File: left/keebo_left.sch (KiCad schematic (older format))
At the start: 56 parts, among them SW1 SW_Push, SW10 SW_Push, SW11 SW_Push, SW12 SW_Push, SW13 SW_Push, SW14 SW_Push, SW17 SW_Push, SW18 SW_Push, SW19 SW_Push, SW2 SW_Push, SW20 SW_Push, SW21 SW_Push, SW22 SW_Push, SW25 SW_Push, SW26 SW_Push, SW27 SW_Push, SW28 SW_Push, SW29 SW_Push, SW3 SW_Push, SW30 SW_Push, SW34 SW_Push, SW35 SW_Push, SW36 SW_Push, SW4 SW_Push, SW5 SW_Push, SW6 SW_Push, SW7 SW_Push, SW9 SW_Push

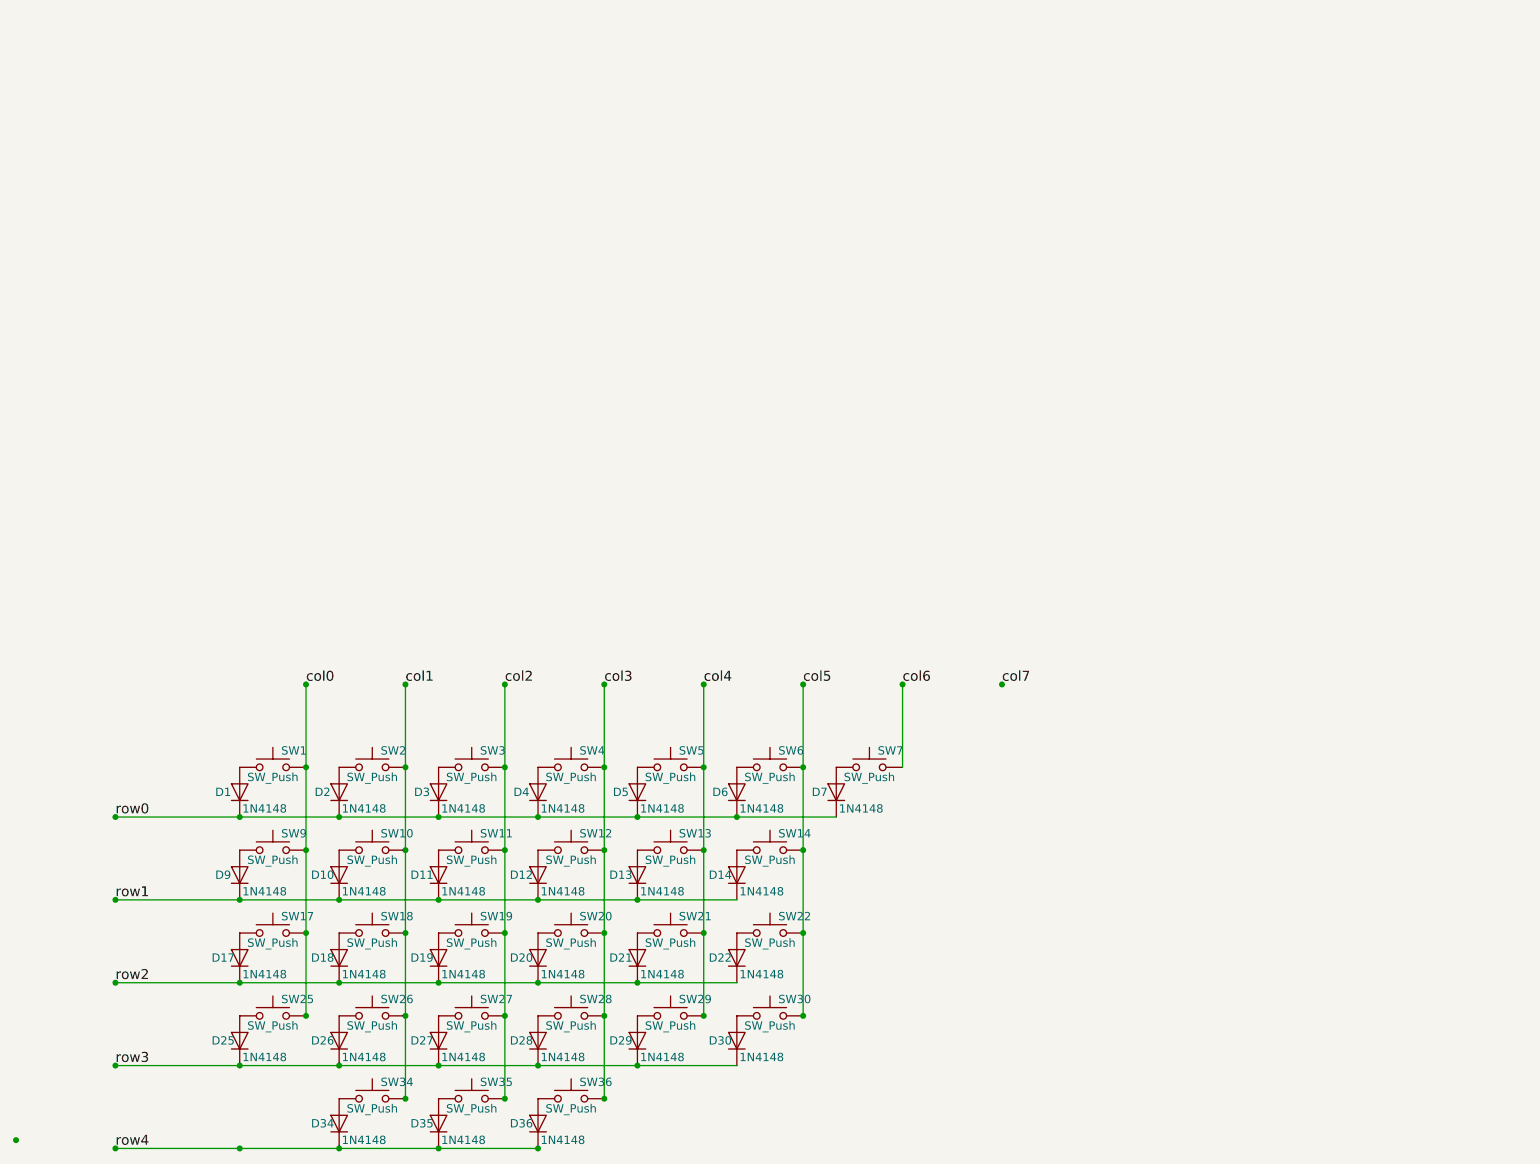
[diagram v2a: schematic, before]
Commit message: Create PCB for low profile switches
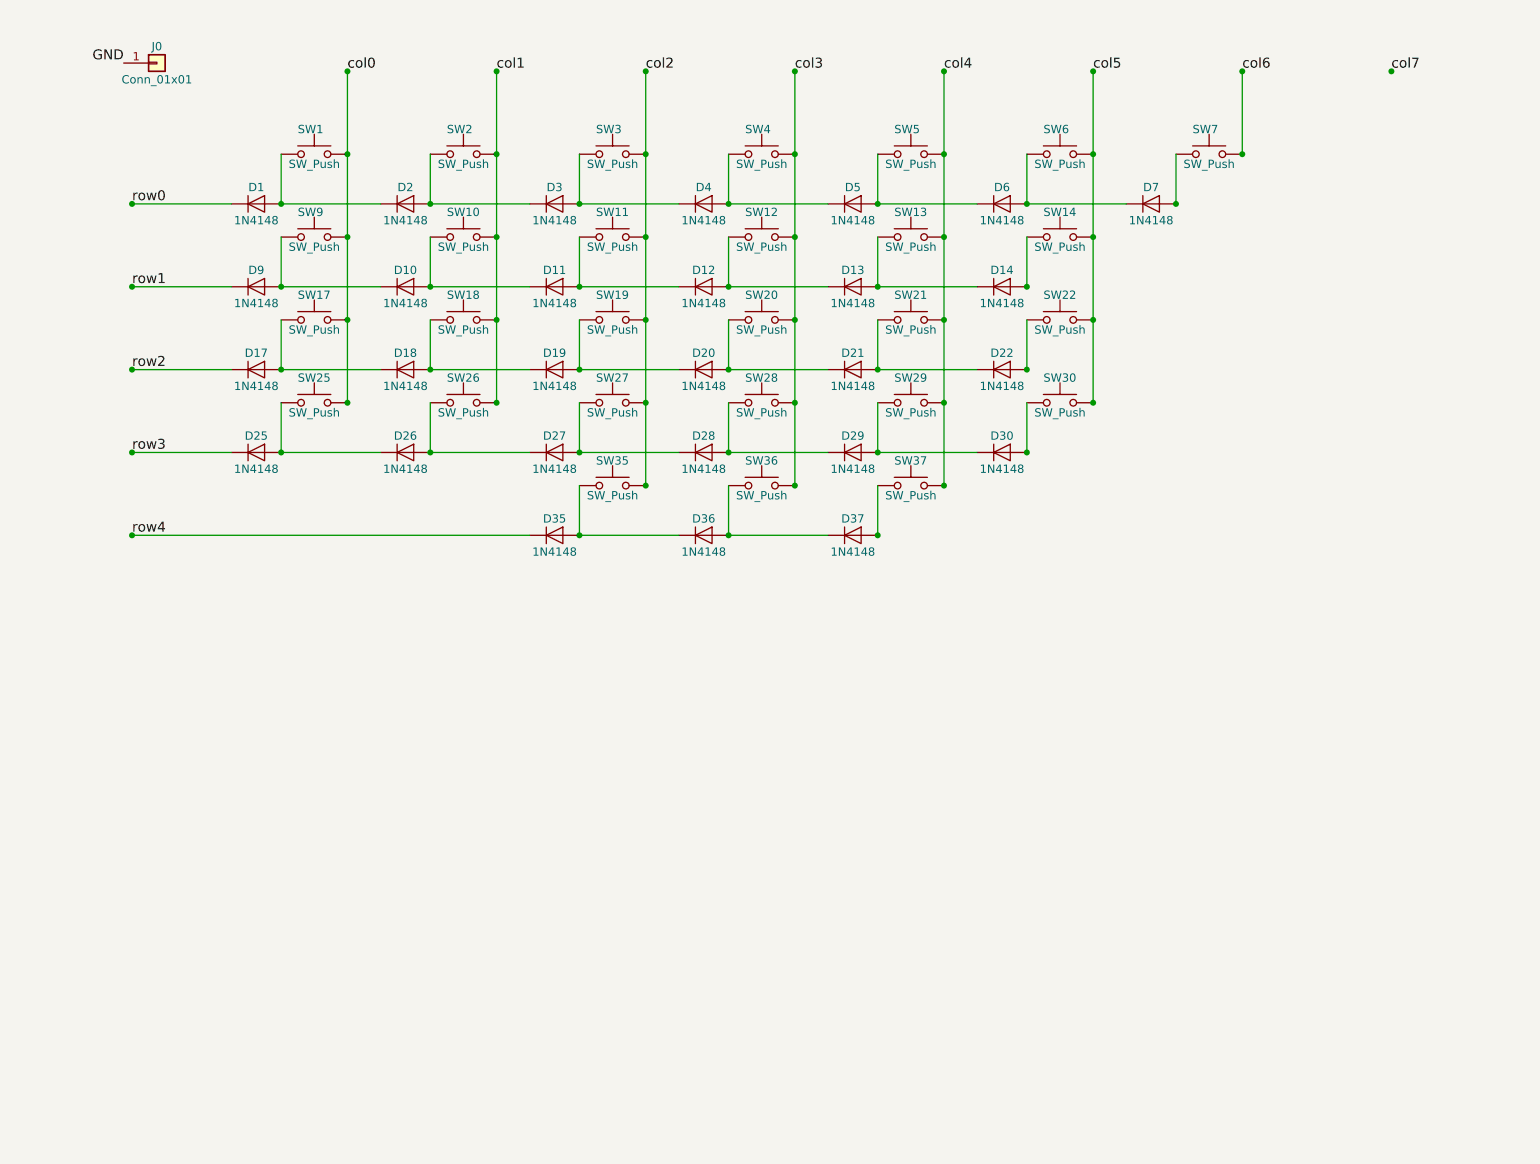
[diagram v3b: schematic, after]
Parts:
- removed D34: 1N4148, Diodes_SMD:D_SOD-123, symbol 1N4148
- removed SW34: SW_Push, keebs:Mx_Alps_125, symbol SW_Push
- added D37: 1N4148, Diodes_SMD:D_SOD-123, symbol 1N4148
- added J0: Conn_01x01, Mounting_Holes:MountingHole_3mm_Pad, symbol Conn_01x01
- added SW37: SW_Push, req:Kailh-PG1350-1u, symbol SW_Push
- SW1, SW10, SW11, SW12, SW13, SW14, SW18, SW19, SW2, SW20, SW21, SW22, SW26, SW27, SW28, SW29, SW3, SW30, SW4, SW5, SW6, SW7: footprint keebs:Mx_Alps_100 -> req:Kailh-PG1350-1u
- SW17: footprint keebs:Mx_Alps_175 -> req:Kailh-PG1350-1u
- SW25: footprint keebs:Mx_Alps_225 -> req:Kailh-PG1350-1u
- SW35, SW36: footprint keebs:Mx_Alps_125 -> req:Kailh-PG1350-1u
- SW9: footprint keebs:Mx_Alps_150 -> req:Kailh-PG1350-1u
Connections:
- net col4: now also SW37.2
- net row0: no longer D2.1 (K), D3.1 (K), D4.1 (K), D5.1 (K), D6.1 (K), D7.1 (K)
- net row1: no longer D10.1 (K), D11.1 (K), D12.1 (K), D13.1 (K), D14.1 (K)
- net row2: no longer D18.1 (K), D19.1 (K), D20.1 (K), D21.1 (K), D22.1 (K)
- net row3: no longer D26.1 (K), D27.1 (K), D28.1 (K), D29.1 (K), D30.1 (K)
- net row4: no longer D36.1 (K)
- net at D1.2 (A), SW1.1: now also D2.1 (K)
- net at D2.2 (A), SW2.1: now also D3.1 (K)
- net at D3.2 (A), SW3.1: now also D4.1 (K)
- net at D4.2 (A), SW4.1: now also D5.1 (K)
- net at D5.2 (A), SW5.1: now also D6.1 (K)
- net at D6.2 (A), SW6.1: now also D7.1 (K)
- net at D9.2 (A), SW9.1: now also D10.1 (K)
- net at D10.2 (A), SW10.1: now also D11.1 (K)
- net at D11.2 (A), SW11.1: now also D12.1 (K)
- net at D12.2 (A), SW12.1: now also D13.1 (K)
- net at D13.2 (A), SW13.1: now also D14.1 (K)
- net at D17.2 (A), SW17.1: now also D18.1 (K)
- net at D18.2 (A), SW18.1: now also D19.1 (K)
- net at D19.2 (A), SW19.1: now also D20.1 (K)
- net at D20.2 (A), SW20.1: now also D21.1 (K)
- net at D21.2 (A), SW21.1: now also D22.1 (K)
- net at D25.2 (A), SW25.1: now also D26.1 (K)
- net at D26.2 (A), SW26.1: now also D27.1 (K)
- net at D27.2 (A), SW27.1: now also D28.1 (K)
- net at D28.2 (A), SW28.1: now also D29.1 (K)
- net at D29.2 (A), SW29.1: now also D30.1 (K)
- net at D35.2 (A), SW35.1: now also D36.1 (K)
- net at D36.2 (A), SW36.1: now also D37.1 (K)
- new net: D37.2 (A), SW37.1
- new net GND: J0.1 (Pin_1)
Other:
- moved on the sheet: D1, SW1

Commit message: Begin recreating standard profile layout
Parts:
- SW1, SW10, SW11, SW12, SW13, SW14, SW18, SW19, SW2, SW20, SW21, SW22, SW26, SW27, SW28, SW29, SW3, SW30, SW4, SW5, SW6, SW7: footprint req:Kailh-PG1350-1u -> req:Mx_Alps_100
- SW17: footprint req:Kailh-PG1350-1u -> req:Mx_Alps_175
- SW25: footprint req:Kailh-PG1350-1u -> req:Mx_Alps_225
- SW35, SW36, SW37: footprint req:Kailh-PG1350-1u -> req:Mx_Alps_125
- SW9: footprint req:Kailh-PG1350-1u -> req:Mx_Alps_150
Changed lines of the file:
@@
 F 0 "SW1" H 1850 1600 50  0000 L CNN
 F 1 "SW_Push" H 1950 1390 50  0000 C CNN
-F 2 "req:Kailh-PG1350-1u" H 1950 1650 50  0001 C CNN
+F 2 "req:Mx_Alps_100" H 1950 1650 50  0001 C CNN
 F 3 "" H 1950 1650 50  0001 C CNN
 	1    1950 1450
@@
 F 0 "SW2" H 2750 1600 50  0000 L CNN
 F 1 "SW_Push" H 2850 1390 50  0000 C CNN
-F 2 "req:Kailh-PG1350-1u" H 2850 1650 50  0001 C CNN
+F 2 "req:Mx_Alps_100" H 2850 1650 50  0001 C CNN
 F 3 "" H 2850 1650 50  0001 C CNN
 	1    2850 1450
@@
 F 0 "SW3" H 3650 1600 50  0000 L CNN
 F 1 "SW_Push" H 3750 1390 50  0000 C CNN
-F 2 "req:Kailh-PG1350-1u" H 3750 1650 50  0001 C CNN
+F 2 "req:Mx_Alps_100" H 3750 1650 50  0001 C CNN
 F 3 "" H 3750 1650 50  0001 C CNN
 	1    3750 1450
@@
 F 0 "SW4" H 4550 1600 50  0000 L CNN
 F 1 "SW_Push" H 4650 1390 50  0000 C CNN
-F 2 "req:Kailh-PG1350-1u" H 4650 1650 50  0001 C CNN
+F 2 "req:Mx_Alps_100" H 4650 1650 50  0001 C CNN
 F 3 "" H 4650 1650 50  0001 C CNN
 	1    4650 1450
@@
 F 0 "SW5" H 5450 1600 50  0000 L CNN
 F 1 "SW_Push" H 5550 1390 50  0000 C CNN
-F 2 "req:Kailh-PG1350-1u" H 5550 1650 50  0001 C CNN
+F 2 "req:Mx_Alps_100" H 5550 1650 50  0001 C CNN
 F 3 "" H 5550 1650 50  0001 C CNN
 	1    5550 1450
@@
 F 0 "SW6" H 6350 1600 50  0000 L CNN
 F 1 "SW_Push" H 6450 1390 50  0000 C CNN
-F 2 "req:Kailh-PG1350-1u" H 6450 1650 50  0001 C CNN
+F 2 "req:Mx_Alps_100" H 6450 1650 50  0001 C CNN
 F 3 "" H 6450 1650 50  0001 C CNN
 	1    6450 1450
@@
 F 0 "SW7" H 7250 1600 50  0000 L CNN
 F 1 "SW_Push" H 7350 1390 50  0000 C CNN
-F 2 "req:Kailh-PG1350-1u" H 7350 1650 50  0001 C CNN
+F 2 "req:Mx_Alps_100" H 7350 1650 50  0001 C CNN
 F 3 "" H 7350 1650 50  0001 C CNN
 	1    7350 1450
@@
 F 0 "SW9" H 1850 2100 50  0000 L CNN
 F 1 "SW_Push" H 1950 1890 50  0000 C CNN
-F 2 "req:Kailh-PG1350-1u" H 1950 2150 50  0001 C CNN
+F 2 "req:Mx_Alps_150" H 1950 2150 50  0001 C CNN
 F 3 "" H 1950 2150 50  0001 C CNN
 	1    1950 1950
@@
 F 0 "SW10" H 2750 2100 50  0000 L CNN
 F 1 "SW_Push" H 2850 1890 50  0000 C CNN
-F 2 "req:Kailh-PG1350-1u" H 2850 2150 50  0001 C CNN
+F 2 "req:Mx_Alps_100" H 2850 2150 50  0001 C CNN
 F 3 "" H 2850 2150 50  0001 C CNN
 	1    2850 1950
@@
 F 0 "SW11" H 3650 2100 50  0000 L CNN
 F 1 "SW_Push" H 3750 1890 50  0000 C CNN
-F 2 "req:Kailh-PG1350-1u" H 3750 2150 50  0001 C CNN
+F 2 "req:Mx_Alps_100" H 3750 2150 50  0001 C CNN
 F 3 "" H 3750 2150 50  0001 C CNN
 	1    3750 1950
@@
 F 0 "SW12" H 4550 2100 50  0000 L CNN
 F 1 "SW_Push" H 4650 1890 50  0000 C CNN
-F 2 "req:Kailh-PG1350-1u" H 4650 2150 50  0001 C CNN
+F 2 "req:Mx_Alps_100" H 4650 2150 50  0001 C CNN
 F 3 "" H 4650 2150 50  0001 C CNN
 	1    4650 1950
@@
 F 0 "SW13" H 5450 2100 50  0000 L CNN
 F 1 "SW_Push" H 5550 1890 50  0000 C CNN
-F 2 "req:Kailh-PG1350-1u" H 5550 2150 50  0001 C CNN
+F 2 "req:Mx_Alps_100" H 5550 2150 50  0001 C CNN
 F 3 "" H 5550 2150 50  0001 C CNN
 	1    5550 1950
@@
 F 0 "SW14" H 6350 2100 50  0000 L CNN
 F 1 "SW_Push" H 6450 1890 50  0000 C CNN
-F 2 "req:Kailh-PG1350-1u" H 6450 2150 50  0001 C CNN
+F 2 "req:Mx_Alps_100" H 6450 2150 50  0001 C CNN
 F 3 "" H 6450 2150 50  0001 C CNN
 	1    6450 1950
@@
 F 0 "SW17" H 1850 2600 50  0000 L CNN
 F 1 "SW_Push" H 1950 2390 50  0000 C CNN
-F 2 "req:Kailh-PG1350-1u" H 1950 2650 50  0001 C CNN
+F 2 "req:Mx_Alps_175" H 1950 2650 50  0001 C CNN
 F 3 "" H 1950 2650 50  0001 C CNN
 	1    1950 2450
@@
 F 0 "SW18" H 2750 2600 50  0000 L CNN
 F 1 "SW_Push" H 2850 2390 50  0000 C CNN
-F 2 "req:Kailh-PG1350-1u" H 2850 2650 50  0001 C CNN
+F 2 "req:Mx_Alps_100" H 2850 2650 50  0001 C CNN
 F 3 "" H 2850 2650 50  0001 C CNN
 	1    2850 2450
@@
 F 0 "SW19" H 3650 2600 50  0000 L CNN
 F 1 "SW_Push" H 3750 2390 50  0000 C CNN
-F 2 "req:Kailh-PG1350-1u" H 3750 2650 50  0001 C CNN
+F 2 "req:Mx_Alps_100" H 3750 2650 50  0001 C CNN
 F 3 "" H 3750 2650 50  0001 C CNN
 	1    3750 2450
@@
 F 0 "SW20" H 4550 2600 50  0000 L CNN
 F 1 "SW_Push" H 4650 2390 50  0000 C CNN
-F 2 "req:Kailh-PG1350-1u" H 4650 2650 50  0001 C CNN
+F 2 "req:Mx_Alps_100" H 4650 2650 50  0001 C CNN
 F 3 "" H 4650 2650 50  0001 C CNN
 	1    4650 2450
@@
 F 0 "SW21" H 5450 2600 50  0000 L CNN
 F 1 "SW_Push" H 5550 2390 50  0000 C CNN
-F 2 "req:Kailh-PG1350-1u" H 5550 2650 50  0001 C CNN
+F 2 "req:Mx_Alps_100" H 5550 2650 50  0001 C CNN
 F 3 "" H 5550 2650 50  0001 C CNN
 	1    5550 2450
@@
 F 0 "SW22" H 6350 2600 50  0000 L CNN
 F 1 "SW_Push" H 6450 2390 50  0000 C CNN
-F 2 "req:Kailh-PG1350-1u" H 6450 2650 50  0001 C CNN
+F 2 "req:Mx_Alps_100" H 6450 2650 50  0001 C CNN
 F 3 "" H 6450 2650 50  0001 C CNN
 	1    6450 2450
@@
 F 0 "SW25" H 1850 3100 50  0000 L CNN
 F 1 "SW_Push" H 1950 2890 50  0000 C CNN
-F 2 "req:Kailh-PG1350-1u" H 1950 3150 50  0001 C CNN
+F 2 "req:Mx_Alps_225" H 1950 3150 50  0001 C CNN
 F 3 "" H 1950 3150 50  0001 C CNN
 	1    1950 2950
@@
 F 0 "SW26" H 2750 3100 50  0000 L CNN
 F 1 "SW_Push" H 2850 2890 50  0000 C CNN
-F 2 "req:Kailh-PG1350-1u" H 2850 3150 50  0001 C CNN
+F 2 "req:Mx_Alps_100" H 2850 3150 50  0001 C CNN
 F 3 "" H 2850 3150 50  0001 C CNN
 	1    2850 2950
@@
 F 0 "SW27" H 3650 3100 50  0000 L CNN
 F 1 "SW_Push" H 3750 2890 50  0000 C CNN
-F 2 "req:Kailh-PG1350-1u" H 3750 3150 50  0001 C CNN
+F 2 "req:Mx_Alps_100" H 3750 3150 50  0001 C CNN
 F 3 "" H 3750 3150 50  0001 C CNN
 	1    3750 2950
@@
 F 0 "SW28" H 4550 3100 50  0000 L CNN
 F 1 "SW_Push" H 4650 2890 50  0000 C CNN
-F 2 "req:Kailh-PG1350-1u" H 4650 3150 50  0001 C CNN
+F 2 "req:Mx_Alps_100" H 4650 3150 50  0001 C CNN
 F 3 "" H 4650 3150 50  0001 C CNN
 	1    4650 2950
@@
 F 0 "SW29" H 5450 3100 50  0000 L CNN
 F 1 "SW_Push" H 5550 2890 50  0000 C CNN
-F 2 "req:Kailh-PG1350-1u" H 5550 3150 50  0001 C CNN
+F 2 "req:Mx_Alps_100" H 5550 3150 50  0001 C CNN
 F 3 "" H 5550 3150 50  0001 C CNN
 	1    5550 2950
@@
 F 0 "SW30" H 6350 3100 50  0000 L CNN
 F 1 "SW_Push" H 6450 2890 50  0000 C CNN
-F 2 "req:Kailh-PG1350-1u" H 6450 3150 50  0001 C CNN
+F 2 "req:Mx_Alps_100" H 6450 3150 50  0001 C CNN
 F 3 "" H 6450 3150 50  0001 C CNN
 	1    6450 2950
@@
 F 0 "SW35" H 3650 3600 50  0000 L CNN
 F 1 "SW_Push" H 3750 3390 50  0000 C CNN
-F 2 "req:Kailh-PG1350-1u" H 3750 3650 50  0001 C CNN
+F 2 "req:Mx_Alps_125" H 3750 3650 50  0001 C CNN
 F 3 "" H 3750 3650 50  0001 C CNN
 	1    3750 3450
@@
 F 0 "SW36" H 4550 3600 50  0000 L CNN
 F 1 "SW_Push" H 4650 3390 50  0000 C CNN
-F 2 "req:Kailh-PG1350-1u" H 4650 3650 50  0001 C CNN
+F 2 "req:Mx_Alps_125" H 4650 3650 50  0001 C CNN
 F 3 "" H 4650 3650 50  0001 C CNN
 	1    4650 3450
@@
 F 0 "SW37" H 5450 3600 50  0000 L CNN
 F 1 "SW_Push" H 5550 3390 50  0000 C CNN
-F 2 "req:Kailh-PG1350-1u" H 5550 3650 50  0001 C CNN
+F 2 "req:Mx_Alps_125" H 5550 3650 50  0001 C CNN
 F 3 "" H 5550 3650 50  0001 C CNN
 	1    5550 3450
